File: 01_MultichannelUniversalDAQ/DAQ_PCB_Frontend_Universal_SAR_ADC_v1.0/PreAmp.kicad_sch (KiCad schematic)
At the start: 41 parts, among them J2 Conn_01x05, U2 LT3092, U3 INA823

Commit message: bugfix
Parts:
- removed R11: 0R, Resistor_SMD:R_0805_2012Metric_Pad1.20x1.40mm_HandSolder, symbol Device:R_Small
- J2: footprint (none) -> Connector_Molex:Molex_KK-254_AE-6410-05A_1x05_P2.54mm_Vertical
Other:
- moved on the sheet: R12

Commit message: Commit after meeting
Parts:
- removed C7: 100n, Capacitor_SMD:C_0603_1608Metric_Pad1.08x0.95mm_HandSolder, symbol Device:C_Small
- removed R14, R15, R29, R30, R31, R32: 0R, Resistor_SMD:R_0805_2012Metric_Pad1.20x1.40mm_HandSolder, symbol Device:R_Small
- removed R19: 100R, Resistor_SMD:R_0805_2012Metric_Pad1.20x1.40mm_HandSolder, symbol Device:R_Small
- removed R35: 10k, Resistor_SMD:R_0603_1608Metric, symbol Device:R
- added C25, C69: 10u, Capacitor_SMD:C_0603_1608Metric_Pad1.08x0.95mm_HandSolder, symbol Device:C_Small
- added R44: 0R, Resistor_SMD:R_0805_2012Metric_Pad1.20x1.40mm_HandSolder, symbol Device:R_Small
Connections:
- net +10V is gone; now on net SEN_VCC+: R18.2
- net SEN_VCC- is gone; now on net GND: J2.2 (Pin_2), R27.2
- net +12V: now also R16.2; no longer C5.1, R13.2, U2.7, U2.8, U3.7 (Vs+)
- net -12V: no longer C6.2, U3.4 (Vs-)
- net 10V: no longer R16.2
- net 2V5: no longer C8.2, U3.5 (Ref)
- net GND: now also C8.2, U3.5 (Ref)
- net SEN_VCC+: now also U2.7, U2.8
- net SGN_IN+: now also C25.2, R44.2; no longer L1.2, R18.1, R20.2, R22.2
- net SGN_IN-: now also C69.2; no longer L2.2
- net at R34.2, U3.6: now also R44.1
- new net: C25.1, L1.2, R18.1, R20.2, R22.2
- new net: C69.1, L2.2
- new net +15V: C5.1, U3.7 (Vs+)
- new net +24V: R13.2
- new net -15V: C6.2, U3.4 (Vs-)
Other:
- note added: "1206"
- moved on the sheet: C2, C3, C4, C8, R13, R16, R17, R20, R24, R25

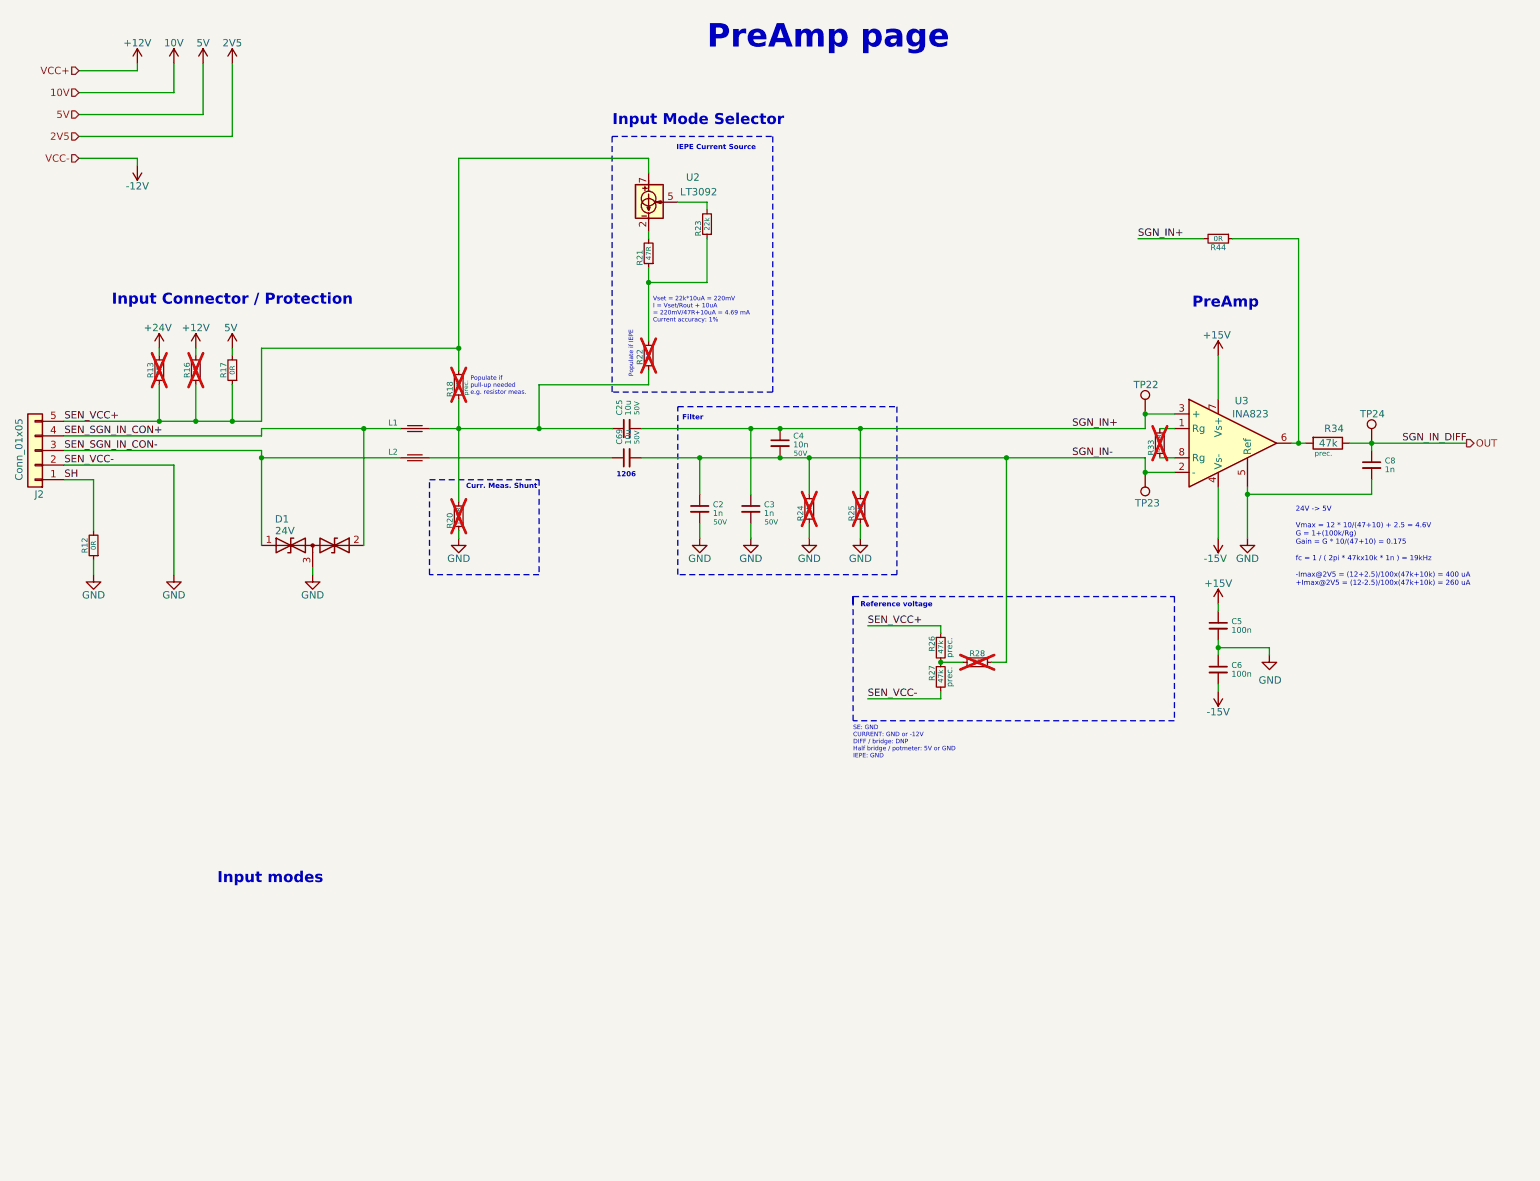
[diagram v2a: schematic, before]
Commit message: ADC és preamp in progress
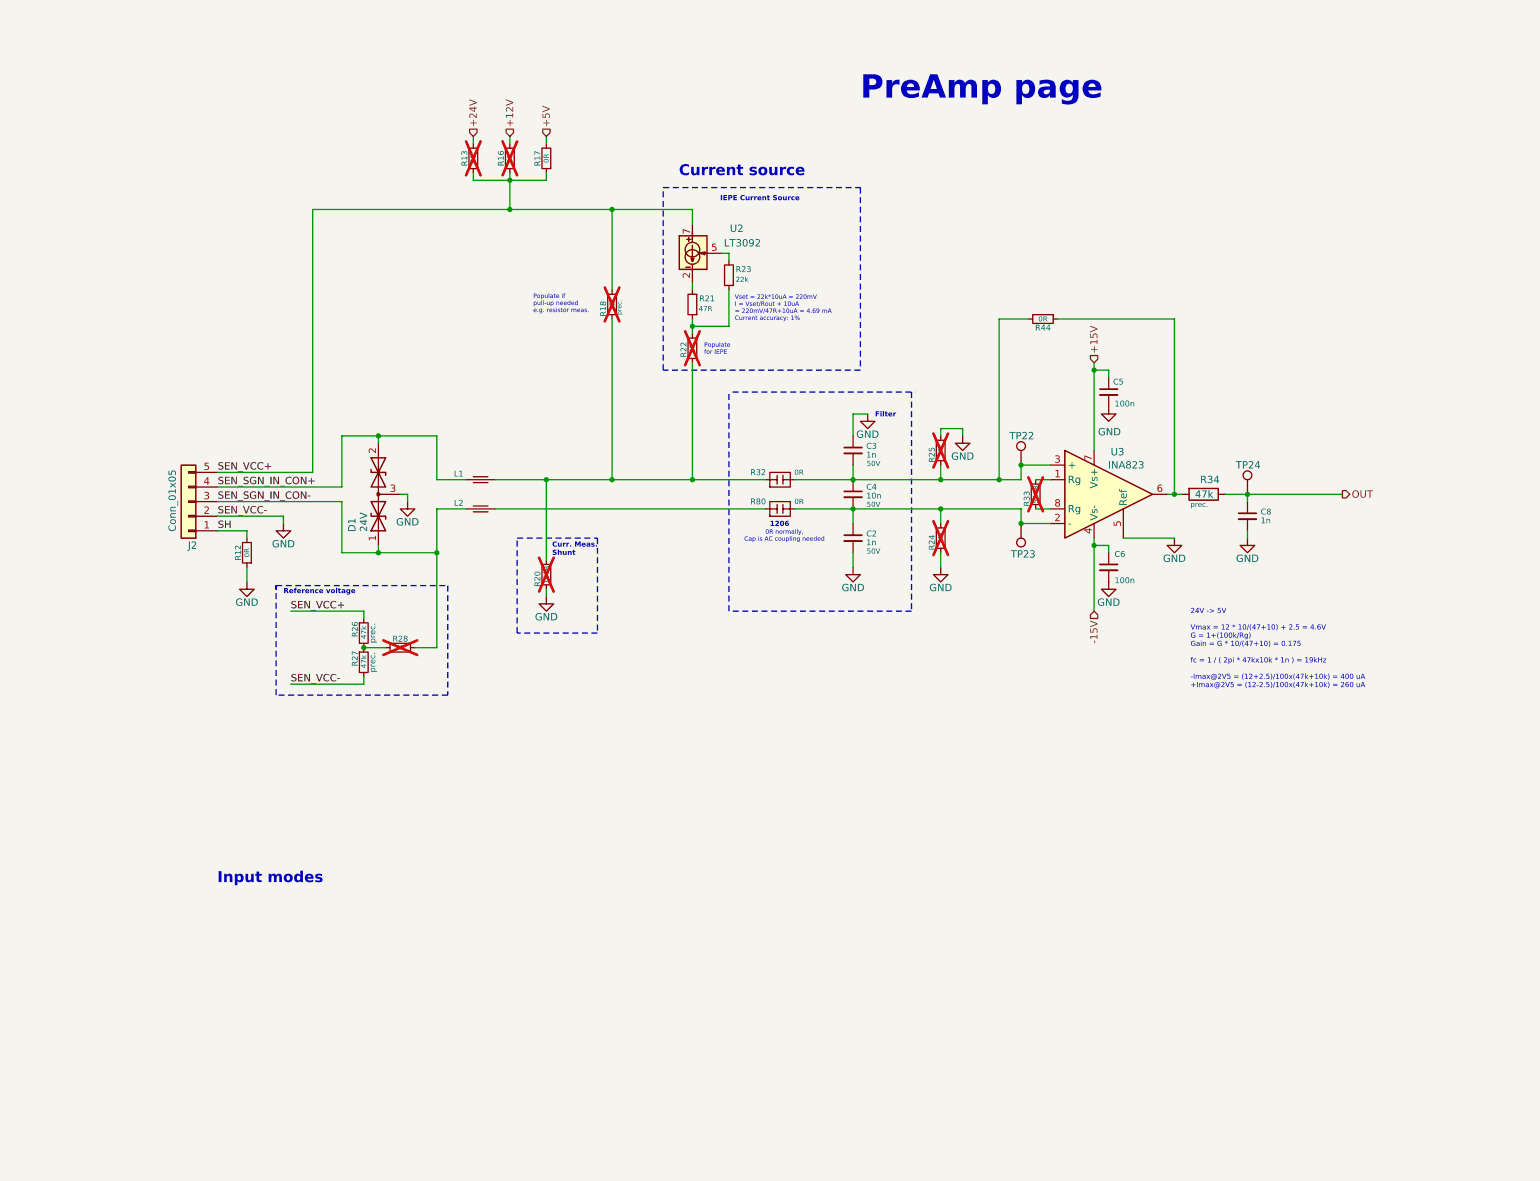
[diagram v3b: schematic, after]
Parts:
- removed C25, C69: 10u, Capacitor_SMD:C_0603_1608Metric_Pad1.08x0.95mm_HandSolder, symbol Device:C_Small
- added R32, R80: 0R, Resistor_SMD:R_0805_2012Metric_Pad1.20x1.40mm_HandSolder, symbol MeMeKicadLib:RC_optional
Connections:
- net -15V: now also C6.1; no longer C6.2
- net GND: now also C3.1, C6.2, R25.2; no longer C3.2, C6.1, R25.1
- net SEN_SGN_IN_CON-: now also R28.2
- net at L1.2, R18.1, R20.2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: now also R32.1
- net at L2.2: now also R80.1
- net 5V renamed +5V
- net SGN_IN+: no longer names the net of C4.1, R44.2, TP22.1, U3.3 (+)
- net SGN_IN+: now also C3.2, R25.1, R32.2; no longer C3.1, R25.2
- net SGN_IN-: no longer names the net of C2.1, C4.2, R24.2, TP23.1, U3.2 (-)
- net SGN_IN-: now also R80.2; no longer R28.2
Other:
- note added: "0R normally, Cap is AC coupling needed"
- note added: "Current source"
- note added: "Populate for IEPE"
- note removed: "Input Connector / Protection"
- note removed: "Input Mode Selector"
- note removed: "Populate if IEPE"
- note removed: "PreAmp"
- note removed: "SE: GND CURRENT: GND or -12V DIFF / bridge: DNP Half bridge / potmeter: 5V or GND IEPE: GND"
- moved on the sheet: C2, C3, C4, C5, C6, C8, D1, J2, L1, L2, R12, R13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

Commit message: ...
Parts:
- renumbered C3 to C20, C4 to C21, C2 to C22, C5 to C23, C6 to C24, C8 to C27, D1 to D3, J2 to J4, L1 to L5, L2 to L6, R12 to R55, R26 to R56, R27 to R57, R28 to R61, R13 to R62, R16 to R63, R17 to R64, R20 to R65, R18 to R66, R21 to R67, R22 to R68, R23 to R70, R32 to R75, R25 to R76, R24 to R77, R33 to R78, R80 to R82, R44 to R86, R34 to R87, TP22 to TP36, TP23 to TP37, TP24 to TP38, U2 to U10, U3 to U11

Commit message: RefBuffer
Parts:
- added R182: 0R, Resistor_SMD:R_0805_2012Metric_Pad1.20x1.40mm_HandSolder, symbol Device:R_Small
- renumbered C23 to C30, C20 to C31, C21 to C32, C27 to C33, C22 to C34, C24 to C35, D3 to D1, J4 to J2, L5 to L1, L6 to L2, R62 to R27, R63 to R28, R64 to R29, R70 to R30, R66 to R31, R67 to R32, R86 to R33, R68 to R34, R76 to R35, R75 to R36, R78 to R37, R87 to R38, R82 to R39, R77 to R40, R55 to R41, R65 to R42, R56 to R43, R61 to R44, R57 to R45, TP36 to TP22, TP38 to TP23, TP37 to TP24, U10 to U4, U11 to U5
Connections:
- net SEN_VCC+: now also R182.1
- new net 4.096V: R182.2
